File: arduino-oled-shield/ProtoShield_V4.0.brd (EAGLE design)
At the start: 68.6 x 53.3 mm, 22 parts

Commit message: oled shield update
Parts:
- added LED1: (no value), led:LED3MM
- added R8: (no value), resistor:0207/10
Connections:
- new net N$24: LED1.A, R8.1
- net GND: now also LED1.K
- net N$1: now also R8.2
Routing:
- net N$1: track 2.54 -> 97.2 mm
- net N$17: track 51.8 -> 61.7 mm
- net N$24: track 0.00 -> 8.06 mm
- net SDA: track 37.2 -> 42.0 mm
- net VCC: track 157.4 -> 162.2 mm
- net N$37: track 45.8 -> 42.3 mm
- net N$5: track 33.0 -> 35.4 mm
- net N$26: track 48.7 -> 46.7 mm
- net SCL: track 42.2 -> 43.7 mm
- net N$33: track 45.9 -> 44.6 mm

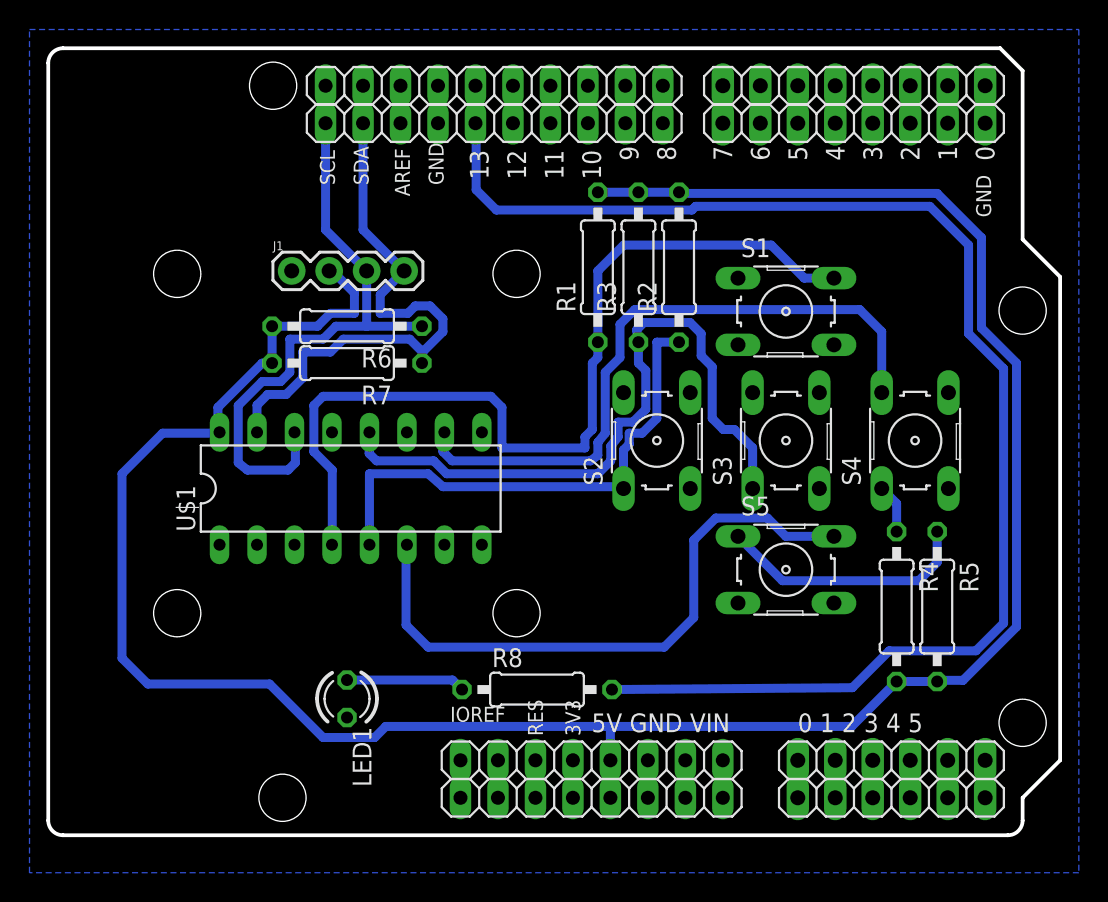
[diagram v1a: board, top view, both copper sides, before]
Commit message: board signal clearance fix
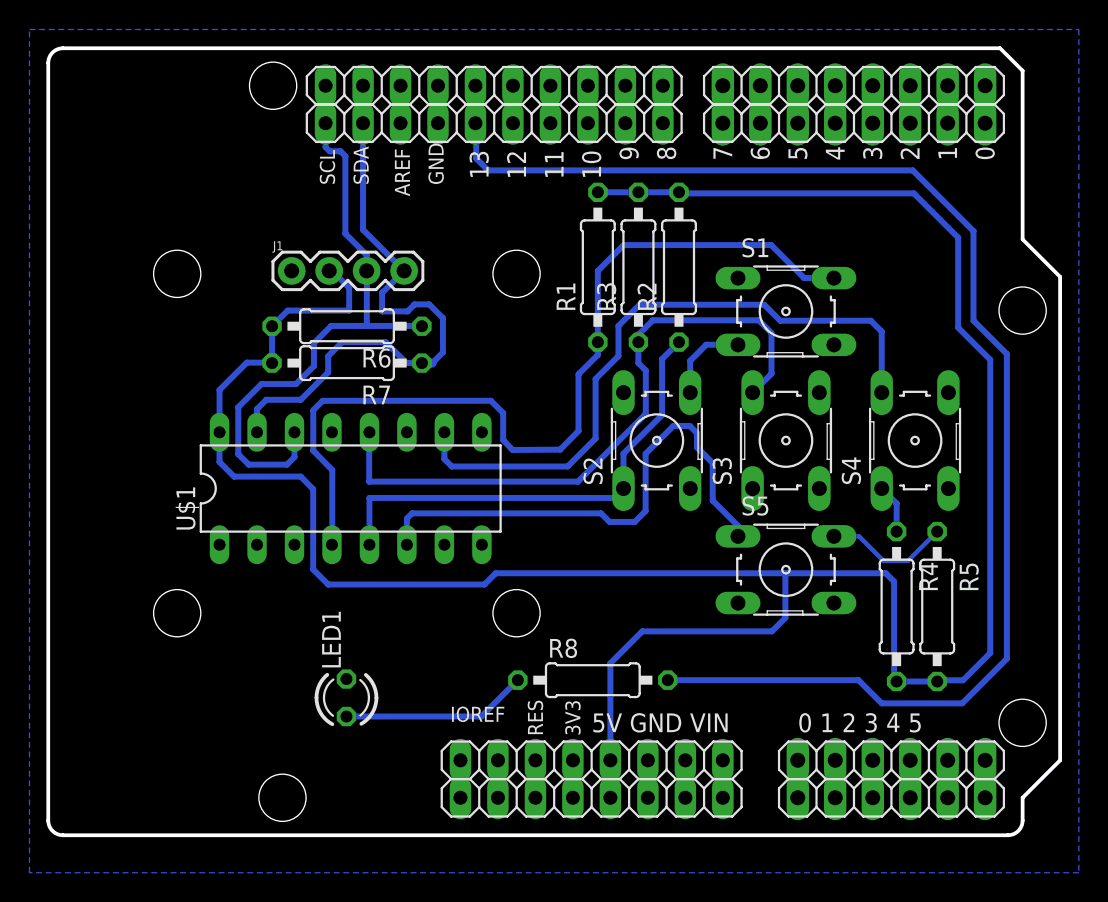
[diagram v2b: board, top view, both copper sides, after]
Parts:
- moved R8 3.84 mm to (36.9, 10.5)
- moved LED1 0.08 mm to (20.2, 9.32), turned to 90 degrees
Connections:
- net GND: now also DIGITAL-H1.7, DIGITAL-H2.7; no longer S1.3, S2.3, S2.4
- net N$16: now also S1.3, S2.4; no longer DIGITAL-H1.7, DIGITAL-H2.7
- net N$26: now also S3.2; no longer S3.1
- net N$31: now also S5.2; no longer S5.1
- net N$37: now also S5.1; no longer S5.2
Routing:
- net N$31: track 17.3 -> 8.51 mm
- net N$37: track 42.3 -> 35.1 mm
- net N$16: track 0.00 -> 5.84 mm
- net VCC: track 162.2 -> 167.8 mm
- net N$24: track 8.06 -> 12.7 mm
- net N$5: track 35.4 -> 32.1 mm
- net N$26: track 46.7 -> 43.9 mm
- net N$36: track 0.00 -> 2.54 mm
- net N$13: track 0.00 -> 2.54 mm
- net N$17: track 61.7 -> 59.9 mm
- net N$1: track 97.2 -> 95.5 mm
- net SCL: track 43.7 -> 42.7 mm
